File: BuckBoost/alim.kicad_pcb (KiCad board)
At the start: 2 copper layers, 14 parts, among them U4 MIC3172YM

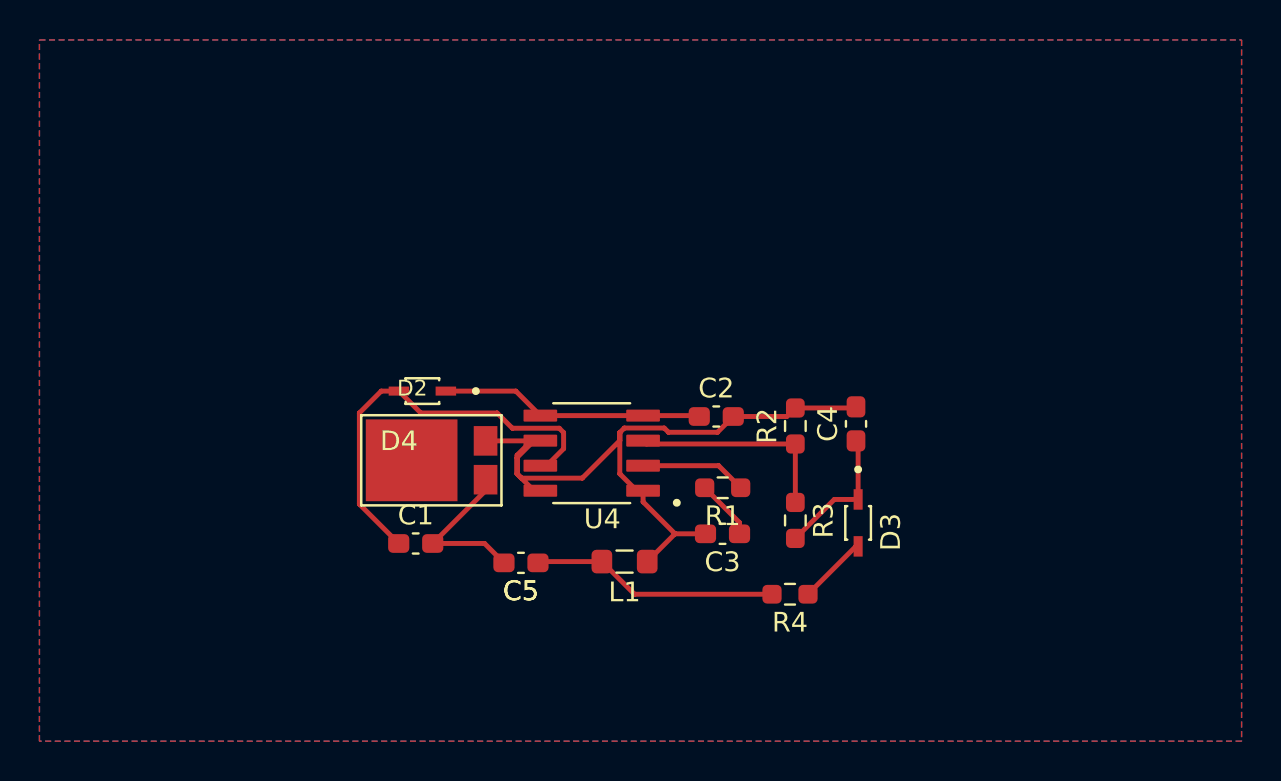
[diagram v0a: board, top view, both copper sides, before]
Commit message: FIN PCB BOOST
Normalement jme suis occupé de l'association de tous les composants et je t'ai fait de la place sur la partie basse du PCB pour le buck
Hésite pas a modifié la taille ou d'autres truc si ça te convient mieux
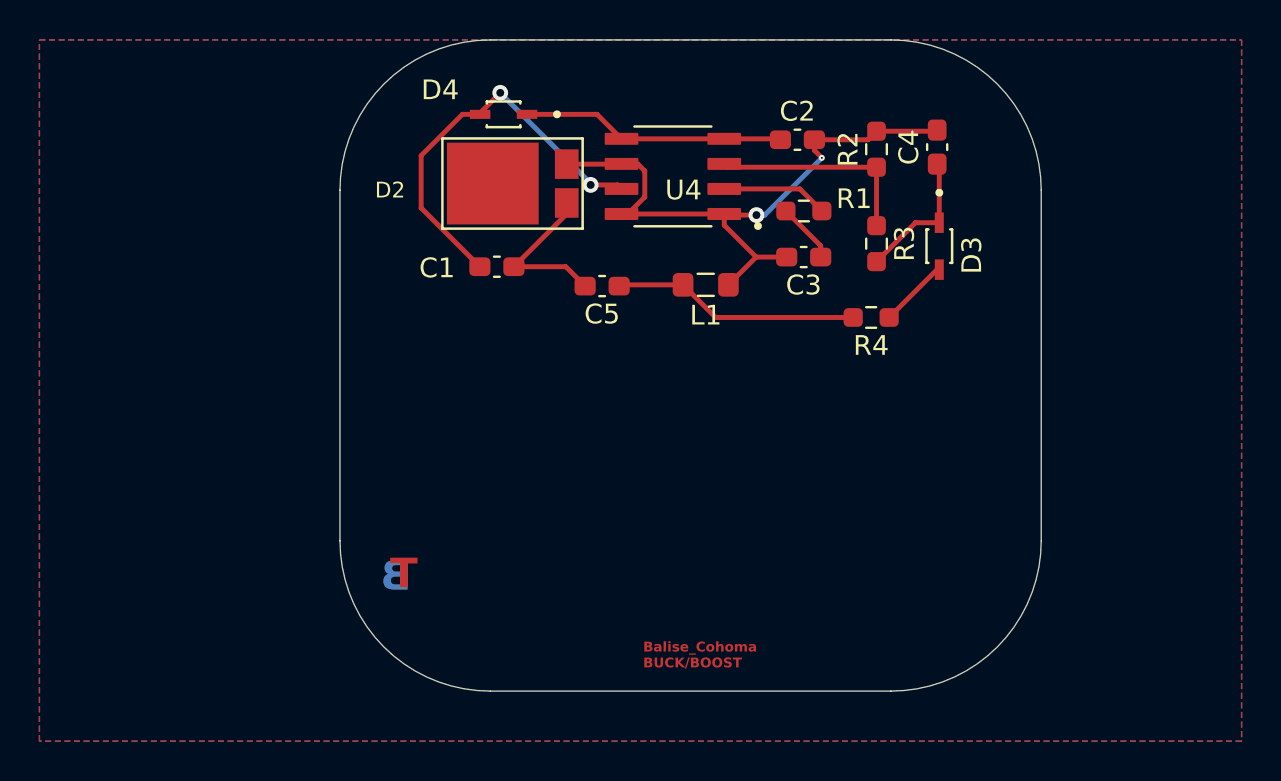
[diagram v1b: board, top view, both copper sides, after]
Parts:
- moved C2 14.6 mm to (142.6, 50.8)
- moved C5 14.6 mm to (132.7, 58.2)
- moved R3 14.6 mm to (146.6, 56.1)
- moved C1 14.6 mm to (127.3, 57.2)
- moved C3 14.6 mm to (142.9, 56.7)
- moved D4 14.6 mm to (127.7, 49.5)
- moved L1 14.6 mm to (137.9, 58.1)
- moved R1 14.6 mm to (142.9, 54.4)
- moved R2 14.6 mm to (146.6, 51.3)
- moved U4 14.6 mm to (136.3, 52.6)
- moved C4 14.6 mm to (149.7, 51.2)
- moved D2 14.6 mm to (128.1, 53.0)
- moved D3 14.6 mm to (149.8, 56.2)
- moved R4 14.6 mm to (146.3, 59.8)
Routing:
- net Net-(D2-K): track 38.3 -> 32.2 mm, vias 0 -> 2
- net Batteries: track 21.5 -> 20.5 mm, vias 0 -> 2
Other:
- board outline added: 35.6 x 33 mm
- board text added: "B"
- board text added: "Balise_Cohoma BUCK/BOOST"
- board text added: "T"
